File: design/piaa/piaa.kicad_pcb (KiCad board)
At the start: 2 copper layers, 152.4 x 53.3 mm, 106 parts, among them J1 Screw_Terminal_01x03, J2 Conn_02x04_Counter_Clockwise, J3 Conn_02x01, J4 Conn_02x01, J5 Conn_02x01, J6 Screw_Terminal_01x06, J7 Screw_Terminal_01x05, J8 Screw_Terminal_01x02, P1 PS2805-4, Q1 FQT13N06L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

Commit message: fix symbols, begin layout
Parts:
- moved F1 164.7 mm to (211.0, 132.8)
- moved F2 164.7 mm to (214.1, 132.8)
- moved F4 164.7 mm to (208.0, 132.8)
- moved F3 161.3 mm to (213.2, 120.8)
- moved F5 161.3 mm to (207.1, 120.8)
- moved F6 161.3 mm to (210.2, 120.8)
- moved Q1 147.0 mm to (192.4, 119.4)
- moved Q3 144.6 mm to (180.3, 116.2)
- moved Q6 141.2 mm to (192.4, 127.6)
- moved Q2 138.8 mm to (191.8, 111.1)
- moved Q5 135.0 mm to (180.3, 126.4)
- moved Q4 134.7 mm to (180.3, 107.3)
- moved U5 119.6 mm to (167.6, 128.9)
- moved U2 117.8 mm to (168.8, 116.2)
- moved U6 117.0 mm to (168.9, 124.5)
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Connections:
- D14 pad 2: Net-(D14-Pad2) -> Net-(F7-Pad1)
- D15 pad 1: (no net) -> GND
- D15 pad 2: (no net) -> Net-(D15-Pad2)
- D17 pad 1: (no net) -> GND
- D17 pad 2: (no net) -> +5V
- F7 pad 1: (no net) -> Net-(F7-Pad1)
- F7 pad 2: (no net) -> Net-(C15-Pad1)
- L1 pad 2: Net-(D15-Pad) -> Net-(D15-Pad2)
- P1 pad 12: (no net) -> /DIN2
- PS1 pad 1: (no net) -> Net-(D7-Pad2)
- PS1 pad 2: (no net) -> Net-(J1-Pad1)
- PS2 pad 1: (no net) -> Net-(D8-Pad2)
- PS2 pad 2: (no net) -> Net-(J1-Pad2)
- Q1 pad 2: GND -> unconnected-(Q1-Pad2)
- Q1 pad 3: Net-(F1-Pad2) -> GND
- Q1 pad 4: (no net) -> Net-(F1-Pad2)
- Q2 pad 2: GND -> unconnected-(Q2-Pad2)
- Q2 pad 3: Net-(F2-Pad2) -> GND
- Q2 pad 4: (no net) -> Net-(F2-Pad2)
- Q3 pad 2: GND -> unconnected-(Q3-Pad2)
- Q3 pad 3: Net-(F3-Pad2) -> GND
- Q3 pad 4: (no net) -> Net-(F3-Pad2)
- Q4 pad 2: GND -> unconnected-(Q4-Pad2)
- Q4 pad 3: Net-(F4-Pad2) -> GND
- Q4 pad 4: (no net) -> Net-(F4-Pad2)
- Q5 pad 2: GND -> unconnected-(Q5-Pad2)
- Q5 pad 3: Net-(F5-Pad2) -> GND
- Q5 pad 4: (no net) -> Net-(F5-Pad2)
- Q6 pad 2: GND -> unconnected-(Q6-Pad2)
- Q6 pad 3: Net-(F6-Pad2) -> GND
- Q6 pad 4: (no net) -> Net-(F6-Pad2)
- U4 pad 3: /DOUT4 -> /DOUT5
- U9 pad 2: Net-(D15-Pad) -> Net-(D15-Pad2)

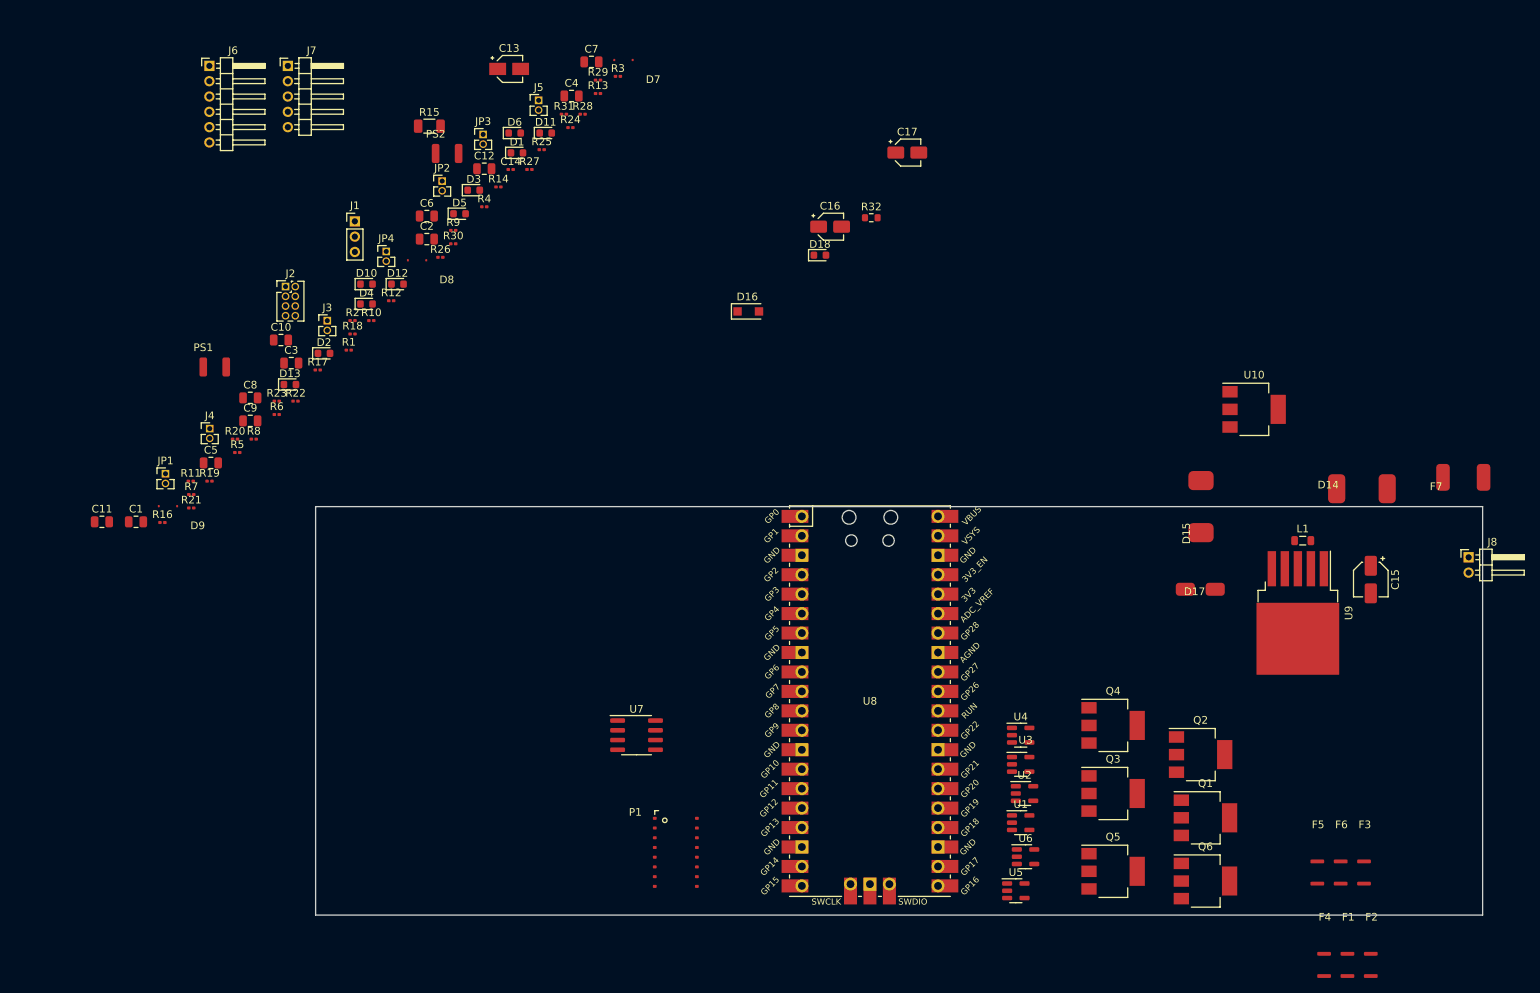
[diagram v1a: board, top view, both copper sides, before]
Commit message: update to pcb drawing
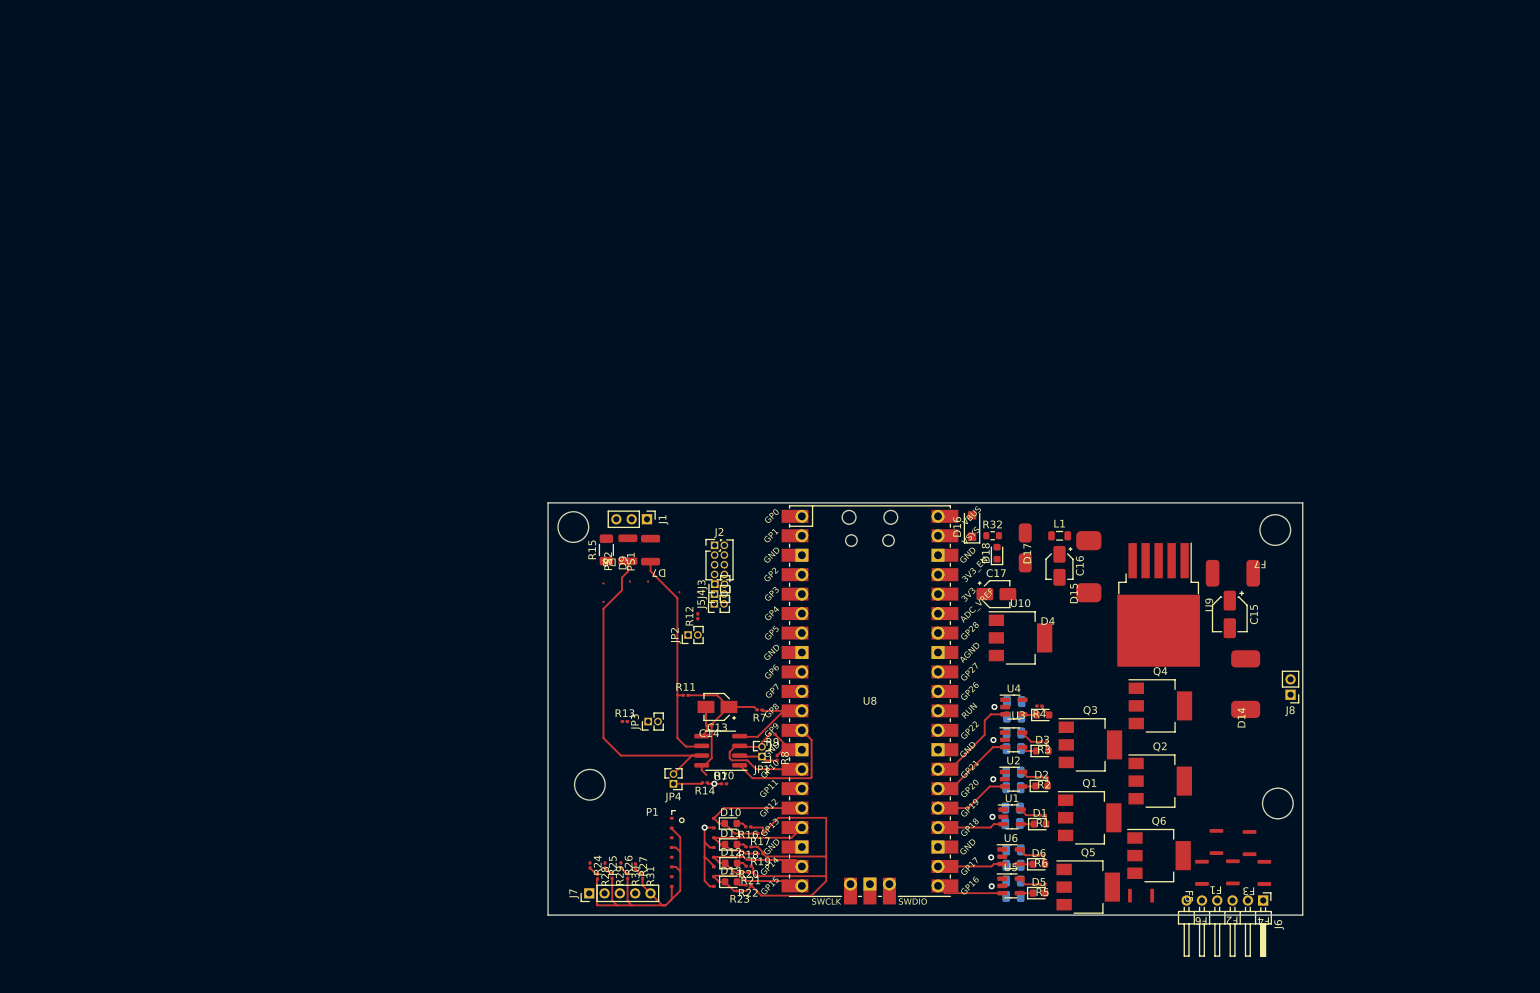
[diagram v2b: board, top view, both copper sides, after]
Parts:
- C1, C10, C11, C12, C2, C3, C4, C5, C6, C7, C8, C9: moved to B.Cu
- J7: footprint Connector_PinHeader_2.00mm:PinHeader_1x05_P2.00mm_Horizontal -> Connector_PinHeader_2.00mm:PinHeader_1x05_P2.00mm_Vertical
- J8: footprint Connector_PinHeader_2.00mm:PinHeader_1x02_P2.00mm_Horizontal -> Connector_PinHeader_2.00mm:PinHeader_1x02_P2.00mm_Vertical
- JP2: value jumper -> RS485A_PU
- moved J6 175.6 mm to (199.9, 130.2), turned to -90 degrees
- moved C11 128.7 mm to (167.3, 129.6)
- moved C1 120.4 mm to (167.2, 118.1)
- moved R5 119.3 mm to (171.1, 128.1), turned to 180 degrees
- moved C5 118.2 mm to (167.3, 127.6)
- moved D6 117.5 mm to (170.7, 125.4)
- moved D5 116.6 mm to (170.7, 129.2)
- moved R6 115.2 mm to (170.9, 124.3), turned to 180 degrees
- moved J7 115.0 mm to (111.9, 129.2), turned to 90 degrees
- moved C6 114.3 mm to (167.3, 125.6)
- moved C7 113.7 mm to (167.2, 120.1)
- moved C12 112.6 mm to (167.3, 123.6)
- moved D1 111.1 mm to (170.8, 120.2)
- moved C8 111.0 mm to (167.3, 113.4)
- moved D2 109.4 mm to (171.0, 115.2)
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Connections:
- J6 pad 1: /OUT0 -> /OUT5
- J6 pad 2: /OUT1 -> /OUT4
- J6 pad 3: /OUT2 -> /OUT3
- J6 pad 4: /OUT3 -> /OUT2
- J6 pad 5: /OUT4 -> /OUT1
- J6 pad 6: /OUT5 -> /OUT0
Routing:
- net +3V3: track 0.00 -> 53.7 mm
- net Net-(D8-Pad2): track 0.00 -> 41.7 mm
- net /COM: track 0.00 -> 40.9 mm
- net GND: track 0.00 -> 38.3 mm, vias 0 -> 2
- net Net-(D7-Pad2): track 0.00 -> 28.9 mm
- net +5V: track 0.00 -> 20.7 mm, vias 0 -> 6
- net /DIN1: track 0.00 -> 18.7 mm
- net /DIN0: track 0.00 -> 18.6 mm
- net /RS485_RX: track 0.00 -> 17.7 mm
- net /RS485_DIR: track 0.00 -> 17.5 mm
- net /DIN2: track 0.00 -> 17.3 mm
- net /DIN3: track 0.00 -> 16.2 mm
- net /RS485_TX: track 0.00 -> 14.8 mm
- net /DOUT5: track 0.00 -> 12.8 mm
- net /DOUT4: track 0.00 -> 11.0 mm
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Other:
- board size 152.4 x 53.3 mm -> 98.6 x 53.8 mm
- board text added: "Maybe best to put MCP1416 on Back copper and Capacitors in front? Evaluate."

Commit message: finalized drawing
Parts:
- moved R10 4.00 mm to (125.6, 114.0), turned to 180 degrees
- moved U10 2.84 mm to (165.5, 96.5), turned to 180 degrees
- moved D18 2.64 mm to (162.6, 85.1)
- moved C17 1.69 mm to (163.4, 89.8), turned to 90 degrees
- moved R32 1.33 mm to (164.1, 83.8), turned to -90 degrees
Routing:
- net GND: track 38.3 -> 280.1 mm, vias 2 -> 17
- net +5V: track 20.7 -> 175.3 mm
- net +3V3: track 53.7 -> 120.6 mm, vias 0 -> 2
- net /GPIO2: track 0.00 -> 27.6 mm
- net Net-(F3-Pad2): track 0.00 -> 26.1 mm
- net Net-(F4-Pad2): track 0.00 -> 25.3 mm
- net /GPIO6: track 0.00 -> 21.3 mm
- net Net-(D15-Pad2): track 0.00 -> 20.8 mm
- net /GPIO4: track 0.00 -> 20.6 mm
- net /GPIO7: track 0.00 -> 20.4 mm
- net Net-(F2-Pad2): track 0.00 -> 17.0 mm
- net Net-(Q6-Pad1): track 2.79 -> 19.0 mm
- net Net-(Q2-Pad1): track 2.81 -> 19.0 mm
- net Net-(Q4-Pad1): track 0.00 -> 15.5 mm
- net Net-(F1-Pad2): track 0.00 -> 14.1 mm
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- added copper zone on B.Cu, net +5V
- added copper zone on B.Cu, net GND
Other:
- board text added: "REMOVE DEBUG SOLDER PADS SO THAT THIS CAN BE USED WITH RASPBERRY PI PICO W! (SWCLK, SWDIO)"

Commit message: add antenna keepout and padding
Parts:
- JP2: value RS485A_PU -> jumper
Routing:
- net +3V3: track 120.6 -> 116.6 mm
- net GND: vias 17 -> 19
- added copper zone on F.Cu, net GND
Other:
- outline, holes or cut-outs redrawn
- board text added: "CYW43439 + Proant Keepout"
- board text removed: "REMOVE DEBUG SOLDER PADS SO THAT THIS CAN BE USED WITH RASPBERRY PI PICO W! (SWCLK, SWDIO)"

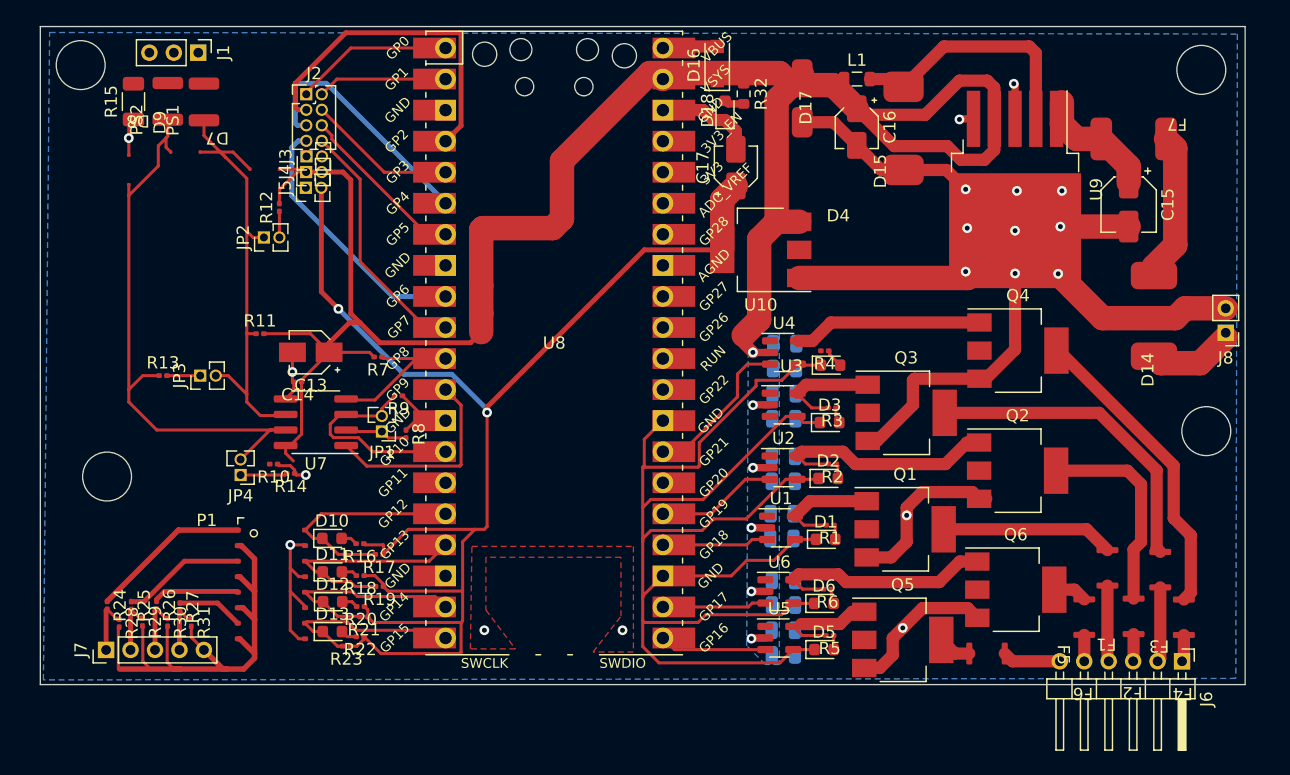
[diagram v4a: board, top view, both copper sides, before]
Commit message: fix header and bornier size
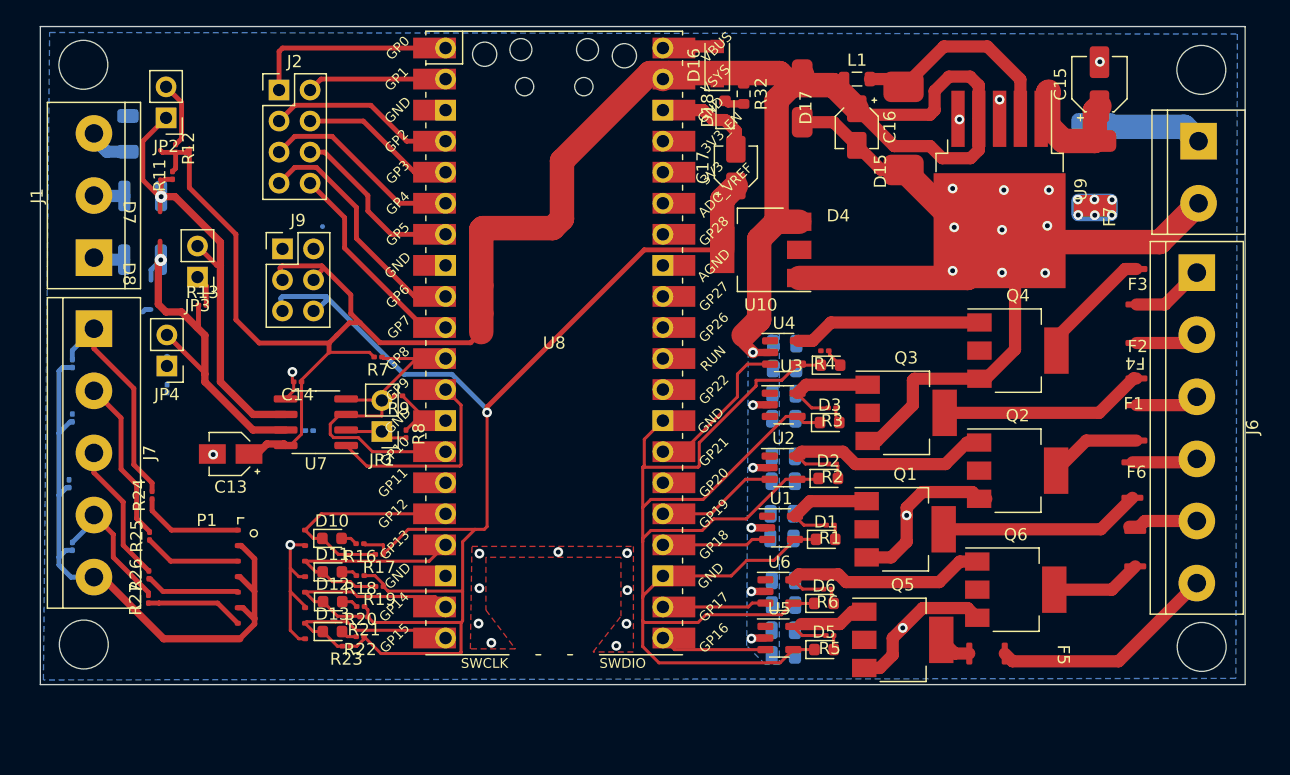
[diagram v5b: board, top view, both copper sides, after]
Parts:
- removed J3, J4, J5: Conn_02x01, Connector_PinHeader_1.27mm:PinHeader_1x02_P1.27mm_Vertical
- added J9: Conn_01x06_Female, Connector_PinHeader_2.54mm:PinHeader_2x03_P2.54mm_Vertical, F.Cu at (126.4, 96.4)
- D14, D9, PS1, PS2, R10, R14, R15, R28, R29, R30, R31: moved to B.Cu
- J1: footprint Connector_PinHeader_2.00mm:PinHeader_1x03_P2.00mm_Vertical -> TerminalBlock:TerminalBlock_bornier-3_P5.08mm
- J2: footprint Connector_PinHeader_1.27mm:PinHeader_2x04_P1.27mm_Vertical -> Connector_PinHeader_2.54mm:PinHeader_2x04_P2.54mm_Vertical
- J6: footprint Connector_PinHeader_2.00mm:PinHeader_1x06_P2.00mm_Horizontal -> TerminalBlock:TerminalBlock_bornier-6_P5.08mm
- J7: footprint Connector_PinHeader_2.00mm:PinHeader_1x05_P2.00mm_Vertical -> TerminalBlock:TerminalBlock_bornier-5_P5.08mm
- J8: footprint Connector_PinHeader_2.00mm:PinHeader_1x02_P2.00mm_Vertical -> TerminalBlock:TerminalBlock_bornier-2_P5.08mm
- JP1, JP2, JP3, JP4: footprint Connector_PinHeader_1.27mm:PinHeader_1x02_P1.27mm_Vertical -> Connector_PinHeader_2.54mm:PinHeader_1x02_P2.54mm_Vertical
- moved J6 31.8 mm to (201.2, 98.4)
- moved F3 28.6 mm to (196.3, 99.8), turned to 0 degrees
- moved F2 27.3 mm to (196.3, 104.9), turned to 0 degrees
- moved F4 27.3 mm to (196.1, 105.3)
- moved J7 26.3 mm to (110.9, 103.0), turned to -90 degrees
- moved R28 21.6 mm to (109.2, 105.8)
- moved D14 21.5 mm to (192.8, 85.4), turned to -90 degrees
- moved F1 18.8 mm to (196.0, 109.6), turned to 0 degrees
- moved J1 18.8 mm to (110.9, 97.2), turned to 90 degrees
- moved F6 17.7 mm to (196.2, 115.2), turned to 0 degrees
- moved R29 17.6 mm to (109.2, 110.3)
- moved J8 15.8 mm to (201.3, 87.6), turned to -90 degrees
- moved R11 14.8 mm to (117.4, 90.4), turned to 90 degrees
- moved R30 13.9 mm to (108.9, 115.6)
- moved JP2 12.6 mm to (116.8, 85.7), turned to 180 degrees
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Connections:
- J1 pad 1: Net-(J1-Pad1) -> Net-(PS2-Pad2)
- J1 pad 2: Net-(J1-Pad2) -> Net-(PS1-Pad2)
- PS1 pad 2: Net-(J1-Pad1) -> Net-(PS1-Pad2)
- PS2 pad 2: Net-(J1-Pad2) -> Net-(PS2-Pad2)
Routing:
- net GND: track 280.1 -> 261.9 mm, vias 19 -> 26
- net Net-(D8-Pad2): track 46.9 -> 30.5 mm, vias 0 -> 1
- net Net-(F4-Pad2): track 25.3 -> 10.1 mm
- net /RS485_TX: track 14.8 -> 0.00 mm
- net /RS485_DIR: track 17.5 -> 32.4 mm
- net /OUT0: track 4.77 -> 18.6 mm
- net /IN0: track 4.68 -> 18.5 mm
- net +5V: track 175.3 -> 187.5 mm
- net Net-(D14-Pad2): track 12.2 -> 0.00 mm, vias 0 -> 6
- net /GPIO2: track 27.6 -> 15.4 mm
- net Net-(F2-Pad2): track 17.0 -> 7.59 mm
- net Net-(F3-Pad2): track 26.1 -> 16.9 mm
- net /IN1: track 4.54 -> 13.5 mm
- net /COM: track 43.5 -> 51.1 mm
- net /IN3: track 4.40 -> 11.4 mm
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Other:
- outline, holes or cut-outs redrawn
